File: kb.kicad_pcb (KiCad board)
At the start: 2 copper layers, 203.2 x 114.3 mm, 188 parts, among them J1 Conn_02x04, J2 10029449-001RLF, J3 Conn_01x05, J4 Conn_01x10, J5 Conn_01x07, J6 Conn_01x06, SW1 RotaryEncoder_Switch, U1 Pico, U2 SN74AHCT125D

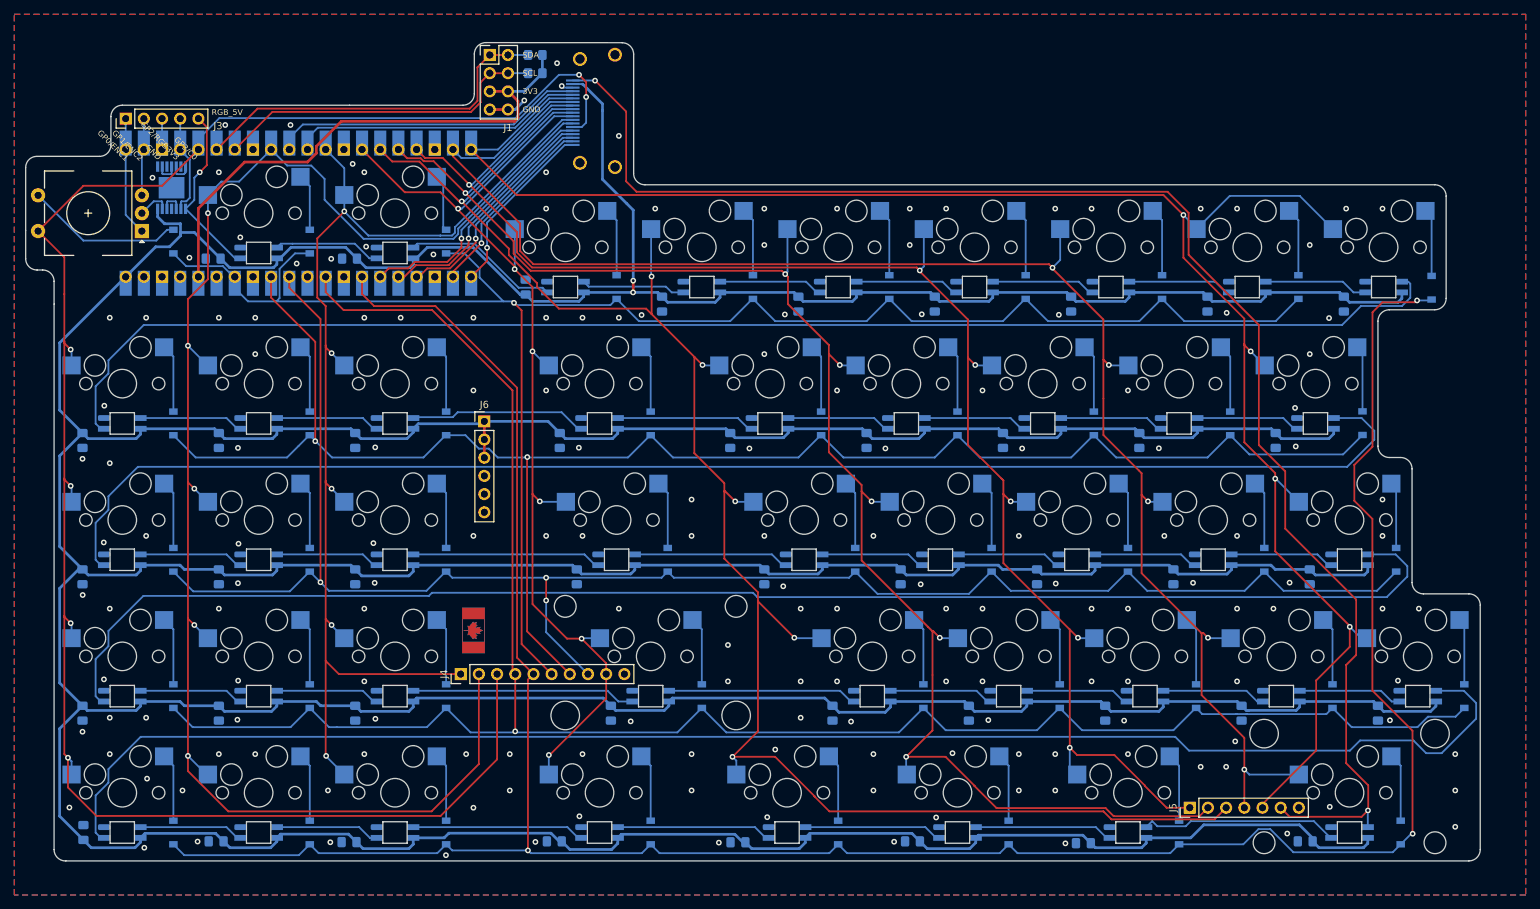
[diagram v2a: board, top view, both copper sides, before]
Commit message: shift hdmi board cutout
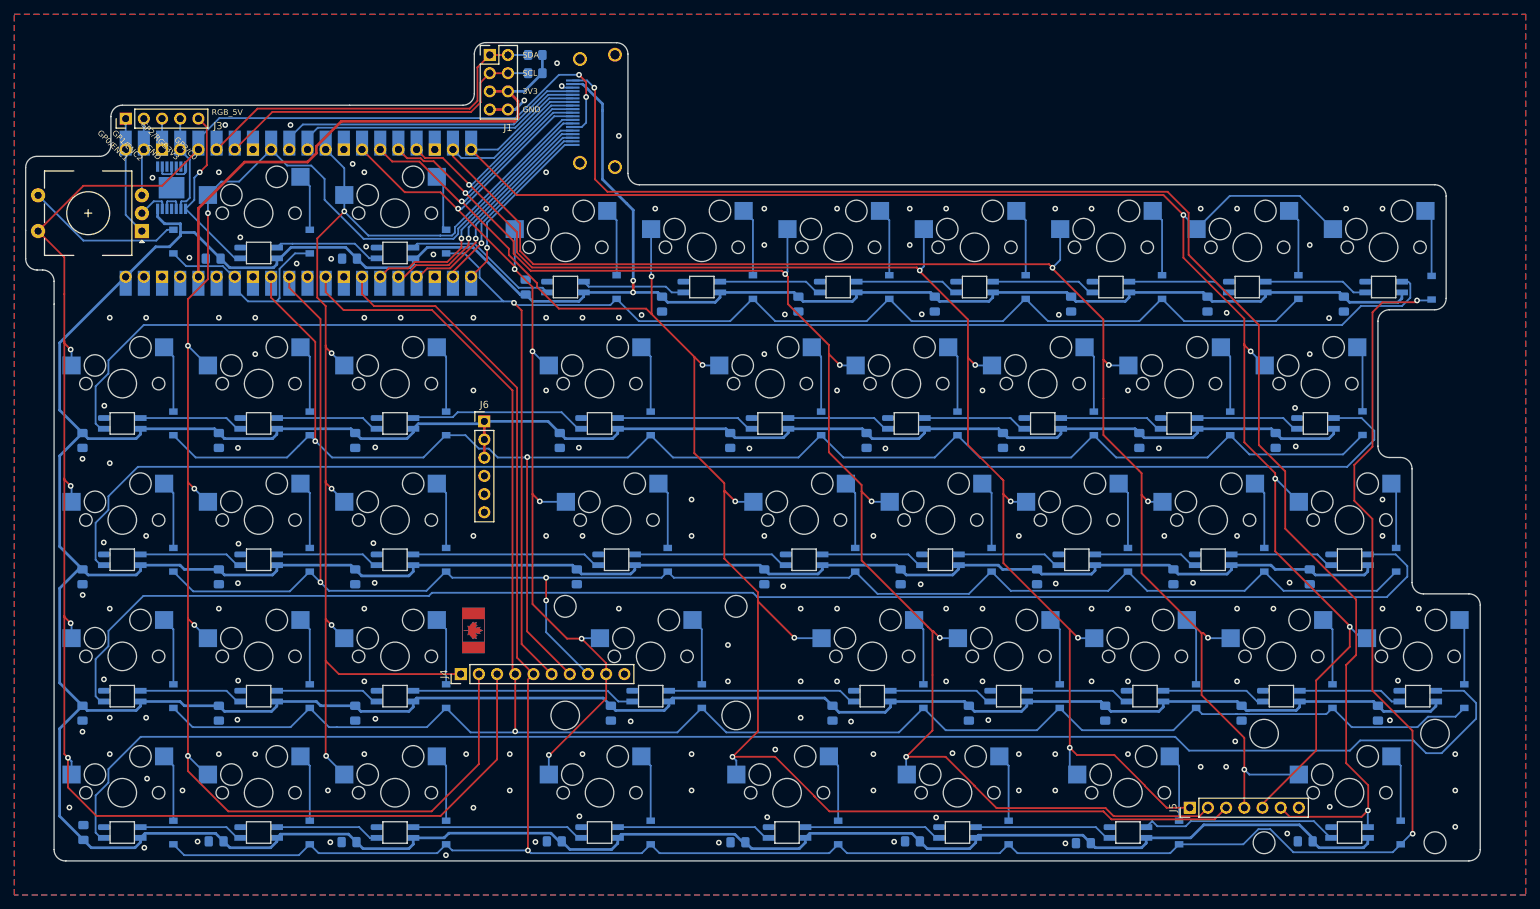
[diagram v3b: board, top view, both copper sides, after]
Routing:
- net /RGB_TO_RIGHT: track 209.9 -> 211.6 mm
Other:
- outline, holes or cut-outs redrawn
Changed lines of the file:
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@@
   (gr_line (start 37.30625 51.59375) (end 69.05625 51.59375) (layer "Edge.Cuts") (width 0.1))
   (gr_line (start 27.78125 76.2) (end 27.78125 79.375) (layer "Edge.Cuts") (width 0.1))
-  (gr_arc (start 107.15625 42.8625) (mid 108.269805 43.336445) (end 108.74375 44.45) (layer "Edge.Cuts") (width 0.1))
+  (gr_arc (start 106.3625 42.8625) (mid 107.480507 43.331993) (end 107.95 44.45) (layer "Edge.Cuts") (width 0.1))
   (gr_line (start 23.8125 69.05625) (end 23.8125 60.325) (layer "Edge.Cuts") (width 0.1))
   (gr_line (start 222.25 64.29375) (end 222.25 78.58125) (layer "Edge.Cuts") (width 0.1))
-  (gr_line (start 88.122485 42.846985) (end 107.15625 42.8625) (layer "Edge.Cuts") (width 0.1))
+  (gr_line (start 88.122485 42.846985) (end 106.3625 42.8625) (layer "Edge.Cuts") (width 0.1))
   (gr_arc (start 86.486999 49.990747) (mid 86.030149 51.115029) (end 84.915003 51.59375) (layer "Edge.Cuts") (width 0.1))
   (gr_line (start 23.8125 69.05625) (end 23.8125 73.025) (layer "Edge.Cuts") (width 0.1))
@@
   (gr_arc (start 35.71875 57.15) (mid 35.253782 58.272532) (end 34.13125 58.7375) (layer "Edge.Cuts") (width 0.1))
   (gr_arc (start 29.419893 157.1625) (mid 28.263188 156.716997) (end 27.78125 155.575) (layer "Edge.Cuts") (width 0.1))
-  (gr_line (start 110.33125 62.70625) (end 220.6625 62.70625) (layer "Edge.Cuts") (width 0.1))
+  (gr_line (start 109.5375 62.706249) (end 220.6625 62.70625) (layer "Edge.Cuts") (width 0.1))
   (gr_arc (start 214.3125 100.80625) (mid 213.189968 100.341282) (end 212.725 99.21875) (layer "Edge.Cuts") (width 0.1))
   (gr_line (start 217.4875 102.39375) (end 217.4875 118.26875) (layer "Edge.Cuts") (width 0.1))
-  (gr_arc (start 110.33125 62.706249) (mid 109.206281 62.243718) (end 108.74375 61.11875) (layer "Edge.Cuts") (width 0.1))
+  (gr_arc (start 109.5375 62.706249) (mid 108.412537 62.243713) (end 107.95 61.11875) (layer "Edge.Cuts") (width 0.1))
   (gr_arc (start 219.075 119.85625) (mid 217.952468 119.391282) (end 217.4875 118.26875) (layer "Edge.Cuts") (width 0.1))
   (gr_line (start 69.05625 51.59375) (end 84.915003 51.59375) (layer "Edge.Cuts") (width 0.1))
   (gr_arc (start 212.725 81.75625) (mid 213.189968 80.633718) (end 214.3125 80.16875) (layer "Edge.Cuts") (width 0.1))
   (gr_arc (start 25.4 74.6125) (mid 24.277468 74.147532) (end 23.8125 73.025) (layer "Edge.Cuts") (width 0.1))
-  (gr_line (start 108.74375 44.45) (end 108.74375 61.11875) (layer "Edge.Cuts") (width 0.1))
+  (gr_line (start 107.95 44.45) (end 107.95 61.11875) (layer "Edge.Cuts") (width 0.1))
   (gr_line (start 212.725 81.75625) (end 212.725 99.21875) (layer "Edge.Cuts") (width 0.1))
   (gr_line (start 86.487 49.990747) (end 86.487 44.434497) (layer "Edge.Cuts") (width 0.1))
@@
   (segment (start 219.36075 66.3575) (end 220.218 67.21475) (width 0.254) (layer "B.Cu") (net 69))
   (segment (start 220.218 67.21475) (end 220.218 75.439) (width 0.254) (layer "B.Cu") (net 69))
-  (segment (start 208.28 129.794) (end 209.677 128.397) (width 0.254) (layer "F.Cu") (net 74))
-  (segment (start 209.677 120.65) (end 199.771 110.744) (width 0.254) (layer "F.Cu") (net 74))
-  (segment (start 209.677 128.397) (end 209.677 120.65) (width 0.254) (layer "F.Cu") (net 74))
-  (segment (start 186.273511 72.481511) (end 186.273511 66.628068) (width 0.254) (layer "F.Cu") (net 74))
-  (segment (start 211.363021 150.078979) (end 211.363021 146.593021) (width 0.254) (layer "F.Cu") (net 74))
-  (segment (start 183.326923 63.68148) (end 109.14748 63.68148) (width 0.254) (layer "F.Cu") (net 74))
-  (segment (start 196.088 99.06) (end 196.088 82.296) (width 0.254) (layer "F.Cu") (net 74))
-  (segment (start 211.328 150.114) (end 211.363021 150.078979) (width 0.254) (layer "F.Cu") (net 74))
-  (segment (start 196.088 82.296) (end 186.273511 72.481511) (width 0.254) (layer "F.Cu") (net 74))
-  (segment (start 186.273511 66.628068) (end 183.326923 63.68148) (width 0.254) (layer "F.Cu") (net 74))
-  (segment (start 107.696 62.23) (end 107.696 52.4764) (width 0.254) (layer "F.Cu") (net 74))
-  (segment (start 199.771 102.743) (end 196.088 99.06) (width 0.254) (layer "F.Cu") (net 74))
-  (segment (start 208.28 143.51) (end 208.28 129.794) (width 0.254) (layer "F.Cu") (net 74))
-  (segment (start 199.771 110.744) (end 199.771 102.743) (width 0.254) (layer "F.Cu") (net 74))
-  (segment (start 109.14748 63.68148) (end 107.696 62.23) (width 0.254) (layer "F.Cu") (net 74))
+  (segment (start 199.771 102.743) (end 199.771 110.744) (width 0.254) (layer "F.Cu") (net 74))
+  (segment (start 103.250815 49.149185) (end 103.3526 49.25097) (width 0.254) (layer "F.Cu") (net 74))
+  (segment (start 103.3526 49.25097) (end 103.3526 61.9506) (width 0.254) (layer "F.Cu") (net 74))
+  (segment (start 208.28 129.794) (end 208.28 143.51) (width 0.254) (layer "F.Cu") (net 74))
+  (segment (start 209.677 120.65) (end 209.677 128.397) (width 0.254) (layer "F.Cu") (net 74))
+  (segment (start 186.273511 72.481511) (end 196.088 82.296) (width 0.254) (layer "F.Cu") (net 74))
+  (segment (start 196.088 99.06) (end 199.771 102.743) (width 0.254) (layer "F.Cu") (net 74))
+  (segment (start 209.677 128.397) (end 208.28 129.794) (width 0.254) (layer "F.Cu") (net 74))
+  (segment (start 199.771 110.744) (end 209.677 120.65) (width 0.254) (layer "F.Cu") (net 74))
+  (segment (start 208.28 143.51) (end 211.363021 146.593021) (width 0.254) (layer "F.Cu") (net 74))
+  (segment (start 103.3526 61.9506) (end 105.08348 63.68148) (width 0.254) (layer "F.Cu") (net 74))
+  (segment (start 186.273511 66.628068) (end 186.273511 72.481511) (width 0.254) (layer "F.Cu") (net 74))
   (segment (start 200.406 151.003) (end 199.136 149.733) (width 0.254) (layer "F.Cu") (net 74))
-  (segment (start 211.363021 146.593021) (end 208.28 143.51) (width 0.254) (layer "F.Cu") (net 74))
-  (segment (start 107.696 52.4764) (end 103.378 48.1584) (width 0.254) (layer "F.Cu") (net 74))
+  (segment (start 105.08348 63.68148) (end 183.326923 63.68148) (width 0.254) (layer "F.Cu") (net 74))
+  (segment (start 196.088 82.296) (end 196.088 99.06) (width 0.254) (layer "F.Cu") (net 74))
+  (segment (start 211.363021 150.078979) (end 211.328 150.114) (width 0.254) (layer "F.Cu") (net 74))
+  (segment (start 211.363021 146.593021) (end 211.363021 150.078979) (width 0.254) (layer "F.Cu") (net 74))
   (segment (start 211.328 150.114) (end 210.439 151.003) (width 0.254) (layer "F.Cu") (net 74))
-  (segment (start 103.378 48.1584) (end 103.3526 48.1584) (width 0.254) (layer "F.Cu") (net 74))
   (segment (start 210.439 151.003) (end 200.406 151.003) (width 0.254) (layer "F.Cu") (net 74))
+  (segment (start 183.326923 63.68148) (end 186.273511 66.628068) (width 0.254) (layer "F.Cu") (net 74))
   (via (at 211.328 150.114) (size 0.8) (drill 0.4) (layers "F.Cu" "B.Cu") (net 74))
-  (via (at 103.3526 48.1584) (size 0.8) (drill 0.4) (layers "F.Cu" "B.Cu") (net 74))
+  (via (at 103.250815 49.149185) (size 0.8) (drill 0.4) (layers "F.Cu" "B.Cu") (net 74))
+  (segment (start 103.250815 49.149185) (end 102.23913 48.1375) (width 0.254) (layer "B.Cu") (net 74))
   (segment (start 211.328 150.114) (end 211.30625 150.13575) (width 0.254) (layer "B.Cu") (net 74))
-  (segment (start 103.3526 48.1584) (end 103.3317 48.1375) (width 0.254) (layer "B.Cu") (net 74))
-  (segment (start 103.3317 48.1375) (end 100.24075 48.1375) (width 0.254) (layer "B.Cu") (net 74))
+  (segment (start 102.23913 48.1375) (end 100.24075 48.1375) (width 0.254) (layer "B.Cu") (net 74))
   (segment (start 211.30625 150.13575) (end 211.30625 152.44375) (width 0.254) (layer "B.Cu") (net 74))
   (segment (start 47.9425 75.565) (end 47.9425 65.995145) (width 0.381) (layer "F.Cu") (net 76))
